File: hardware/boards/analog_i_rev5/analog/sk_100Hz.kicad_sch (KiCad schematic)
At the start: 6 parts, among them U20001 OPA333xxDBV

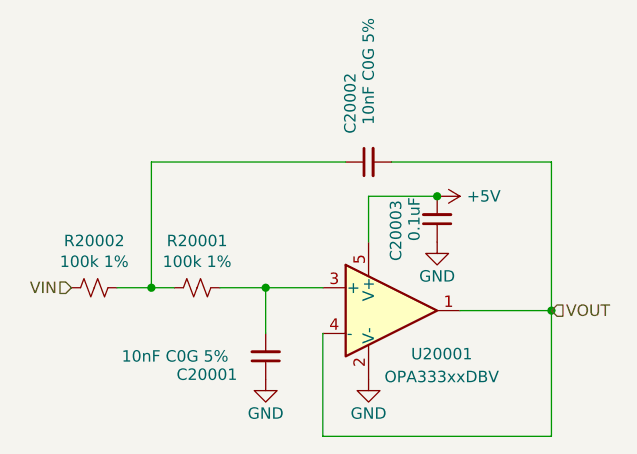
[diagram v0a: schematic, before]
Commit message: update schematic with active filters and overvoltage protection
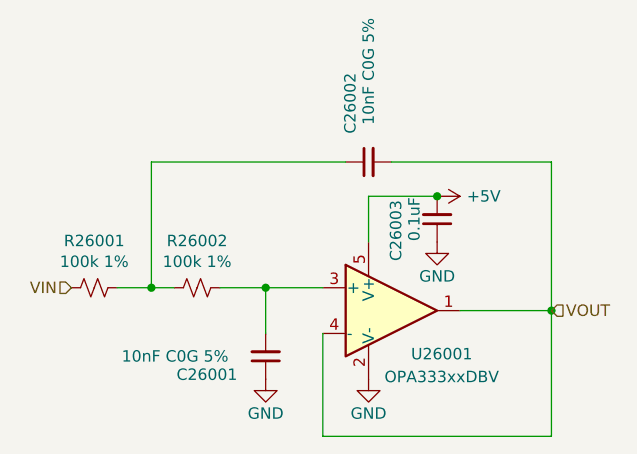
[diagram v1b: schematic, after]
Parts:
- R26001: renamed from R20002; footprint Capacitor_SMD:C_0402_1005Metric -> Resistor_SMD:R_0402_1005Metric
- R26002: renamed from R20001; footprint Capacitor_SMD:C_0402_1005Metric -> Resistor_SMD:R_0402_1005Metric
- renumbered C20001 to C26001, C20002 to C26002, C20003 to C26003, U20001 to U26001
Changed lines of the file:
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@@
 		(on_board yes)
 		(dnp no)
-		(property "Reference" "C20003"
+		(property "Reference" "C26003"
 			(at 116.078 76.2 90)
 			(effects
@@
 		(on_board yes)
 		(dnp no)
-		(property "Reference" "C20001"
+		(property "Reference" "C26001"
 			(at 91.694 92.202 0)
 			(effects
@@
 		(on_board yes)
 		(dnp no)
-		(property "Reference" "C20002"
+		(property "Reference" "C26002"
 			(at 110.998 58.674 0)
 			(effects
@@
 		(on_board yes)
 		(dnp no)
-		(property "Reference" "#PWR20002"
+		(property "Reference" "#PWR26002"
 			(at 113.03 99.06 0)
 			(effects
@@
 		(on_board yes)
 		(dnp no)
-		(property "Reference" "R20001"
+		(property "Reference" "R26002"
 			(at 93.98 77.343 90)
 			(effects
@@
 			)
 		)
-		(property "Footprint" "Capacitor_SMD:C_0402_1005Metric"
+		(property "Footprint" "Resistor_SMD:R_0402_1005Metric"
 			(at 93.98 82.55 0)
 			(effects
@@
 		(on_board yes)
 		(dnp no)
-		(property "Reference" "U20001"
+		(property "Reference" "U26001"
 			(at 121.158 89.916 0)
 			(effects
@@
 		(on_board yes)
 		(dnp no)
-		(property "Reference" "#PWR20004"
+		(property "Reference" "#PWR26004"
 			(at 120.65 83.82 0)
 			(effects
@@
 		(on_board yes)
 		(dnp no)
-		(property "Reference" "R20002"
+		(property "Reference" "R26001"
 			(at 82.55 77.343 90)
 			(effects
@@
 			)
 		)
-		(property "Footprint" "Capacitor_SMD:C_0402_1005Metric"
+		(property "Footprint" "Resistor_SMD:R_0402_1005Metric"
 			(at 82.55 82.55 0)
 			(effects
@@
 		(dnp no)
 		(fields_autoplaced yes)
-		(property "Reference" "#PWR20003"
+		(property "Reference" "#PWR26003"
 			(at 116.84 72.39 0)
 			(effects
@@
 		(on_board yes)
 		(dnp no)
-		(property "Reference" "#PWR20001"
+		(property "Reference" "#PWR26001"
 			(at 101.6 99.06 0)
 			(effects

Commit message: limit amp voltage outputs to 3.3V
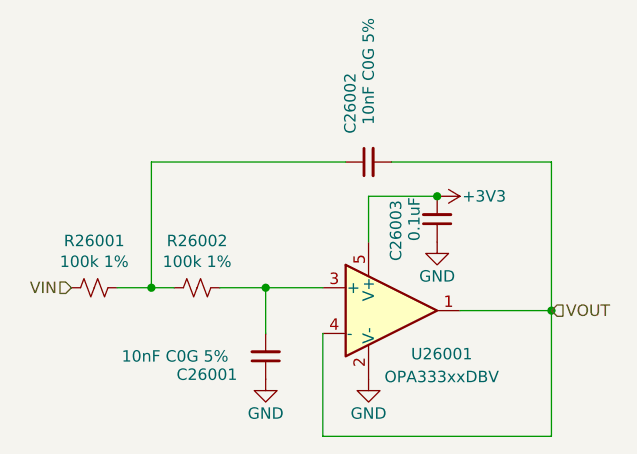
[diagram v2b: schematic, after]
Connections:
- net +5V renamed +3V3
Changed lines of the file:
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@@
+	)
+	(symbol
+		(lib_id "power:+3V3")
+		(at 120.65 72.39 270)
+		(unit 1)
+		(exclude_from_sim no)
+		(in_bom yes)
+		(on_board yes)
+		(dnp no)
+		(property "Reference" "#PWR20003"
+			(at 116.84 72.39 0)
+			(effects
+				(font
+					(size 1.27 1.27)
+				)
+				(hide yes)
+			)
+		)
+		(property "Value" "+3V3"
+			(at 123.444 72.39 90)
+			(effects
+				(font
+					(size 1.27 1.27)
+				)
+				(justify left)
+			)
+		)
+		(property "Footprint" ""
+			(at 120.65 72.39 0)
+			(effects
+				(font
+					(size 1.27 1.27)
+				)
+				(hide yes)
+			)
+		)
+		(property "Datasheet" ""
+			(at 120.65 72.39 0)
+			(effects
+				(font
+					(size 1.27 1.27)
+				)
+				(hide yes)
+			)
+		)
+		(property "Description" "Power symbol creates a global label with name \"+3V3\""
+			(at 120.65 72.39 0)
+			(effects
+				(font
+					(size 1.27 1.27)
+				)
+				(hide yes)
+			)
+		)
+		(pin "1"
+		)
+		(instances
+			(project "analog_frontend_panel"
+				(path "/c241d083-1323-4b4a-a540-956d0afb7b72/3222a655-275a-45ec-a7e7-0c882d3cca28"
+					(reference "#PWR25001")
+					(unit 1)
+				)
+				(path "/c241d083-1323-4b4a-a540-956d0afb7b72/f31a785a-aa18-4b99-9461-7c34b37be0d7"
+					(reference "#PWR20003")
+					(unit 1)
+				)
+			)
+		)
 	)
 	(symbol
@@
 					(unit 1)
 				)
-			)
-		)
-	)
-	(symbol
-		(lib_id "power:+5V")
-		(at 120.65 72.39 270)
-		(unit 1)
-		(exclude_from_sim no)
-		(in_bom yes)
-		(on_board yes)
-		(dnp no)
-		(fields_autoplaced yes)
-		(property "Reference" "#PWR26003"
-			(at 116.84 72.39 0)
-			(effects
-				(font
-					(size 1.27 1.27)
-				)
-				(hide yes)
-			)
-		)
-		(property "Value" "+5V"
-			(at 123.952 72.3899 90)
-			(effects
-				(font
-					(size 1.27 1.27)
-				)
-				(justify left)
-			)
-		)
-		(property "Footprint" ""
-			(at 120.65 72.39 0)
-			(effects
-				(font
-					(size 1.27 1.27)
-				)
-				(hide yes)
-			)
-		)
-		(property "Datasheet" ""
-			(at 120.65 72.39 0)
-			(effects
-				(font
-					(size 1.27 1.27)
-				)
-				(hide yes)
-			)
-		)
-		(property "Description" "Power symbol creates a global label with name \"+5V\""
-			(at 120.65 72.39 0)
-			(effects
-				(font
-					(size 1.27 1.27)
-				)
-				(hide yes)
-			)
-		)
-		(pin "1"
-		)
-		(instances
-			(project "analog_frontend_panel"
-				(path "/c241d083-1323-4b4a-a540-956d0afb7b72/3222a655-275a-45ec-a7e7-0c882d3cca28"
-					(reference "#PWR26003")
-					(unit 1)
-				)
-				(path "/c241d083-1323-4b4a-a540-956d0afb7b72/f31a785a-aa18-4b99-9461-7c34b37be0d7"
-					(reference "#PWR20003")
-					(unit 1)
-				)

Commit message: clean up new schematic
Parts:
- renumbered C26001 to C20001, C26002 to C20002, C26003 to C20003, R26002 to R20001, R26001 to R20002, U26001 to U20001
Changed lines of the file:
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@@
 		(on_board yes)
 		(dnp no)
-		(property "Reference" "C26003"
+		(property "Reference" "C20003"
 			(at 116.078 76.2 90)
 			(effects
@@
 		(instances
 			(project "analog_frontend_panel"
-				(path "/c241d083-1323-4b4a-a540-956d0afb7b72/3222a655-275a-45ec-a7e7-0c882d3cca28"
-					(reference "C26003")
-					(unit 1)
-				)
 				(path "/c241d083-1323-4b4a-a540-956d0afb7b72/f31a785a-aa18-4b99-9461-7c34b37be0d7"
 					(reference "C20003")
+					(unit 1)
+				)
+				(path "/c241d083-1323-4b4a-a540-956d0afb7b72/ed60502d-2e6d-4293-85f2-5e967a3c42d8/63cb4c21-96ec-4930-8398-5e4d00a3dfaf"
+					(reference "C14003")
 					(unit 1)
 				)
@@
 		(on_board yes)
 		(dnp no)
-		(property "Reference" "C26001"
+		(property "Reference" "C20001"
 			(at 91.694 92.202 0)
 			(effects
@@
 		(instances
 			(project "analog_frontend_panel"
-				(path "/c241d083-1323-4b4a-a540-956d0afb7b72/3222a655-275a-45ec-a7e7-0c882d3cca28"
-					(reference "C26001")
-					(unit 1)
-				)
 				(path "/c241d083-1323-4b4a-a540-956d0afb7b72/f31a785a-aa18-4b99-9461-7c34b37be0d7"
 					(reference "C20001")
+					(unit 1)
+				)
+				(path "/c241d083-1323-4b4a-a540-956d0afb7b72/ed60502d-2e6d-4293-85f2-5e967a3c42d8/63cb4c21-96ec-4930-8398-5e4d00a3dfaf"
+					(reference "C14001")
 					(unit 1)
 				)
@@
 		(on_board yes)
 		(dnp no)
-		(property "Reference" "C26002"
+		(property "Reference" "C20002"
 			(at 110.998 58.674 0)
 			(effects
@@
 		(instances
 			(project "analog_frontend_panel"
-				(path "/c241d083-1323-4b4a-a540-956d0afb7b72/3222a655-275a-45ec-a7e7-0c882d3cca28"
-					(reference "C26002")
-					(unit 1)
-				)
 				(path "/c241d083-1323-4b4a-a540-956d0afb7b72/f31a785a-aa18-4b99-9461-7c34b37be0d7"
 					(reference "C20002")
+					(unit 1)
+				)
+				(path "/c241d083-1323-4b4a-a540-956d0afb7b72/ed60502d-2e6d-4293-85f2-5e967a3c42d8/63cb4c21-96ec-4930-8398-5e4d00a3dfaf"
+					(reference "C14002")
 					(unit 1)
 				)
@@
 		(on_board yes)
 		(dnp no)
-		(property "Reference" "#PWR26002"
+		(property "Reference" "#PWR20002"
 			(at 113.03 99.06 0)
 			(effects
@@
 		(instances
 			(project "analog_frontend_panel"
-				(path "/c241d083-1323-4b4a-a540-956d0afb7b72/3222a655-275a-45ec-a7e7-0c882d3cca28"
-					(reference "#PWR26002")
-					(unit 1)
-				)
 				(path "/c241d083-1323-4b4a-a540-956d0afb7b72/f31a785a-aa18-4b99-9461-7c34b37be0d7"
 					(reference "#PWR20002")
+					(unit 1)
+				)
+				(path "/c241d083-1323-4b4a-a540-956d0afb7b72/ed60502d-2e6d-4293-85f2-5e967a3c42d8/63cb4c21-96ec-4930-8398-5e4d00a3dfaf"
+					(reference "#PWR14002")
 					(unit 1)
 				)
@@
 		(on_board yes)
 		(dnp no)
-		(property "Reference" "R26002"
+		(property "Reference" "R20001"
 			(at 93.98 77.343 90)
 			(effects
@@
 		(instances
 			(project "analog_frontend_panel"
-				(path "/c241d083-1323-4b4a-a540-956d0afb7b72/3222a655-275a-45ec-a7e7-0c882d3cca28"
-					(reference "R26002")
-					(unit 1)
-				)
 				(path "/c241d083-1323-4b4a-a540-956d0afb7b72/f31a785a-aa18-4b99-9461-7c34b37be0d7"
 					(reference "R20001")
+					(unit 1)
+				)
+				(path "/c241d083-1323-4b4a-a540-956d0afb7b72/ed60502d-2e6d-4293-85f2-5e967a3c42d8/63cb4c21-96ec-4930-8398-5e4d00a3dfaf"
+					(reference "R14002")
 					(unit 1)
 				)
@@
 		(instances
 			(project "analog_frontend_panel"
-				(path "/c241d083-1323-4b4a-a540-956d0afb7b72/3222a655-275a-45ec-a7e7-0c882d3cca28"
-					(reference "#PWR25001")
-					(unit 1)
-				)
 				(path "/c241d083-1323-4b4a-a540-956d0afb7b72/f31a785a-aa18-4b99-9461-7c34b37be0d7"
 					(reference "#PWR20003")
+					(unit 1)
+				)
+				(path "/c241d083-1323-4b4a-a540-956d0afb7b72/ed60502d-2e6d-4293-85f2-5e967a3c42d8/63cb4c21-96ec-4930-8398-5e4d00a3dfaf"
+					(reference "#PWR14003")
 					(unit 1)
 				)
@@
 		(on_board yes)
 		(dnp no)
-		(property "Reference" "U26001"
+		(property "Reference" "U20001"
 			(at 121.158 89.916 0)
 			(effects
@@
 		(instances
 			(project "analog_frontend_panel"
-				(path "/c241d083-1323-4b4a-a540-956d0afb7b72/3222a655-275a-45ec-a7e7-0c882d3cca28"
-					(reference "U26001")
-					(unit 1)
-				)
 				(path "/c241d083-1323-4b4a-a540-956d0afb7b72/f31a785a-aa18-4b99-9461-7c34b37be0d7"
 					(reference "U20001")
+					(unit 1)
+				)
+				(path "/c241d083-1323-4b4a-a540-956d0afb7b72/ed60502d-2e6d-4293-85f2-5e967a3c42d8/63cb4c21-96ec-4930-8398-5e4d00a3dfaf"
+					(reference "U14001")
 					(unit 1)
 				)
@@
 		(on_board yes)
 		(dnp no)
-		(property "Reference" "#PWR26004"
+		(property "Reference" "#PWR20004"
 			(at 120.65 83.82 0)
 			(effects
@@
 		(instances
 			(project "analog_frontend_panel"
-				(path "/c241d083-1323-4b4a-a540-956d0afb7b72/3222a655-275a-45ec-a7e7-0c882d3cca28"
-					(reference "#PWR26004")
-					(unit 1)
-				)
 				(path "/c241d083-1323-4b4a-a540-956d0afb7b72/f31a785a-aa18-4b99-9461-7c34b37be0d7"
 					(reference "#PWR20004")
+					(unit 1)
+				)
+				(path "/c241d083-1323-4b4a-a540-956d0afb7b72/ed60502d-2e6d-4293-85f2-5e967a3c42d8/63cb4c21-96ec-4930-8398-5e4d00a3dfaf"
+					(reference "#PWR14004")
 					(unit 1)
 				)
@@
 		(on_board yes)
 		(dnp no)
-		(property "Reference" "R26001"
+		(property "Reference" "R20002"
 			(at 82.55 77.343 90)
 			(effects
@@
 		(instances
 			(project "analog_frontend_panel"
-				(path "/c241d083-1323-4b4a-a540-956d0afb7b72/3222a655-275a-45ec-a7e7-0c882d3cca28"
-					(reference "R26001")
-					(unit 1)
-				)
 				(path "/c241d083-1323-4b4a-a540-956d0afb7b72/f31a785a-aa18-4b99-9461-7c34b37be0d7"
 					(reference "R20002")
+					(unit 1)
+				)
+				(path "/c241d083-1323-4b4a-a540-956d0afb7b72/ed60502d-2e6d-4293-85f2-5e967a3c42d8/63cb4c21-96ec-4930-8398-5e4d00a3dfaf"
+					(reference "R14001")
 					(unit 1)
 				)
@@
 		(on_board yes)
 		(dnp no)
-		(property "Reference" "#PWR26001"
+		(property "Reference" "#PWR20001"
 			(at 101.6 99.06 0)
 			(effects
@@
 		(instances
 			(project "analog_frontend_panel"
-				(path "/c241d083-1323-4b4a-a540-956d0afb7b72/3222a655-275a-45ec-a7e7-0c882d3cca28"
-					(reference "#PWR26001")
-					(unit 1)
-				)
 				(path "/c241d083-1323-4b4a-a540-956d0afb7b72/f31a785a-aa18-4b99-9461-7c34b37be0d7"
 					(reference "#PWR20001")
 					(unit 1)
 				)
+				(path "/c241d083-1323-4b4a-a540-956d0afb7b72/ed60502d-2e6d-4293-85f2-5e967a3c42d8/63cb4c21-96ec-4930-8398-5e4d00a3dfaf"
+					(reference "#PWR14001")
+					(unit 1)
+				)

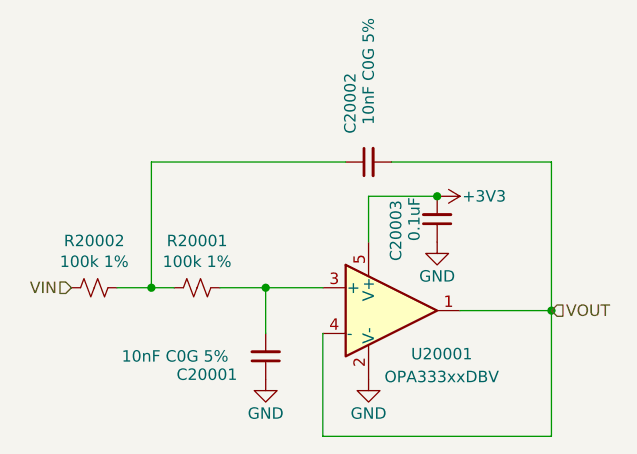
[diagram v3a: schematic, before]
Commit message: shorten board and update combined layout
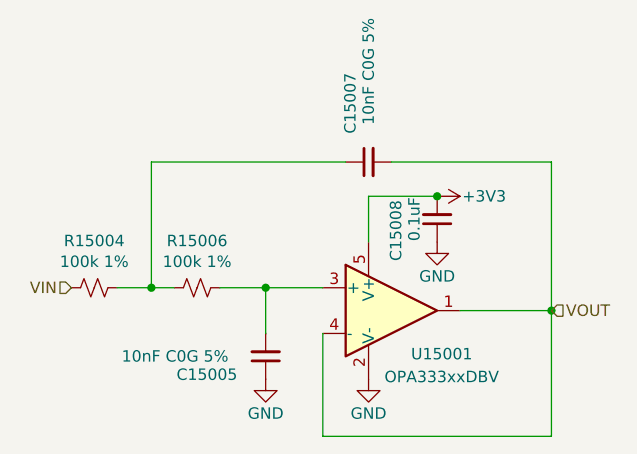
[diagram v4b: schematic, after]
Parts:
- removed C20003: 0.1uF, Capacitor_SMD:C_0402_1005Metric, symbol Device:C_Small
- removed U20001: OPA333xxDBV, Package_TO_SOT_SMD:SOT-23-5, symbol Amplifier_Operational:OPA333xxDBV
- added C15008: 0.1uF, Capacitor_SMD:C_0402_1005Metric, symbol Device:C_Small
- added U15001: OPA333xxDBV, Package_TO_SOT_SMD:SOT-23-5, symbol Amplifier_Operational:OPA333xxDBV
- renumbered C20001 to C15005, C20002 to C15007, R20002 to R15004, R20001 to R15006
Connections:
- net +3V3: now also C15008.2, U15001.5 (V+)
- net GND: now also C15008.1, U15001.2 (V-)
- net VOUT: now also U15001.1, U15001.4 (-)
- net at C15005.2, R15006.1: now also U15001.3 (+)
